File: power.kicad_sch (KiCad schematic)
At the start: 0 parts

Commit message: Connectors done, WIP on power
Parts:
- added C1: 100uF/16V, symbol Device:C_Polarized_Small
- added C10, C7: 0.1uF/50V, Capacitor_SMD:C_0603_1608Metric_Pad1.05x0.95mm_HandSolder, symbol Device:C
- added C11: 10pF/50V, Capacitor_SMD:C_0603_1608Metric_Pad1.05x0.95mm_HandSolder, symbol Device:C
- added C12, C13: 22uF/6.3V, Capacitor_Tantalum_SMD:CP_EIA-3216-10_Kemet-I_Pad1.58x1.35mm_HandSolder, symbol cellar-rescue:CP-Device
- added C2: 47nF/50V, symbol Device:C_Small
- added C3, C4: 1F / 8.1V, Capacitors:SCMR22J105SRBA0_vertical, symbol cellar-rescue:CP-Device
- added C5, C6: 10uF/25V, Capacitor_SMD:C_0805_2012Metric_Pad1.15x1.40mm_HandSolder, symbol Device:C
- added C8: 1uF/25V, Capacitor_SMD:C_0805_2012Metric_Pad1.15x1.40mm_HandSolder, symbol Device:C
- added C9: 8200pF/50V, Capacitor_SMD:C_0603_1608Metric_Pad1.05x0.95mm_HandSolder, symbol Device:C
- added D1: D, symbol Device:D
- added D2, D3, D4: SBR160S23-7, symbol Device:D
- added L1: 1.5uH, Inductors:L_7.1x6.5_H3, symbol cellar-rescue:INDUCTOR-pspice
- added Q1, Q2: Q_NPN_BEC, symbol Device:Q_NPN_BEC
- added R10: 22.1k, symbol Device:R
- added R11, R12: 30, symbol Device:R
- added R13, R3, R7, R9: 100k, symbol Device:R
- added R14: 124k 1%, symbol Device:R
- added R15: 22.1k 1%, symbol Device:R
- added R4, R8: 10k, symbol Device:R
- added R5: 37.4k, symbol Device:R
- added R6: 750k, symbol Device:R
- added U1: TLC555CDR, Package_SO:SOIC-8_3.9x4.9mm_P1.27mm, symbol Timer:TLC555xD
- added U2: L78L33ACUTR, Package_TO_SOT_SMD:SOT-89-3, symbol Regulator_Linear:L78L33_SOT89
- added U3: TPS54625, symbol power_custom:TPS54625
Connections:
- new net: C3.1, D4.2 (A), R11.1, R12.1
- new net: C3.2, C4.1
- new net: C11.2, R14.2, R15.1, U3.2 (VFB)
- new net: Q2.2 (E), R7.2, U1.4 (R)
- new net: Q2.3 (C), R8.1, U2.1 (OUT)
- new net: C10.1, U3.12 (VBST)
- new net: C10.2, L1.1, U3.10 (SW), U3.11 (SW)
- new net: C9.1, U3.4 (SS)
- new net: D2.1 (K), R11.2, R12.2
- new net: C2.1, U1.5 (CV)
- new net: D1.2 (A), R5.1, R6.2, U1.7 (DIS)
- new net: C8.1, R13.2, U3.3 (VREG5)
- new net: R13.1, U3.6 (PG)
- new net: R4.1, U1.3 (Q)
- new net: Q1.1 (B), R4.2
- new net +12V: D2.2 (A), D3.2 (A), R9.1, U2.3 (IN)
- new net +5V: C11.1, C12.1, C13.1, L1.2, R14.1, U3.1 (VO)
- new net ENABLE: Q1.3 (C), R3.2, U3.7 (EN)
- new net GND: C1.2, C12.2, C13.2, C2.2, C4.2, C5.2, C6.2, C7.2, C8.2, C9.2, Q1.2 (E), R10.2, R15.2, R7.1, U1.1 (GND), U2.2 (GND), U3.15 (GND), U3.5 (GND), U3.8 (GND), U3.9 (GND)
- new net POWER_STATE: R10.1, R9.2
- new net THR: C1.1, D1.1 (K), R6.1, U1.2 (TR), U1.6 (THR)
- new net VCOND: C5.1, C6.1, C7.1, D3.1 (K), D4.1 (K), R3.1, R5.2, U1.8 (VCC), U3.13 (VIN), U3.14 (VIN)
- new net WATCHDOG: Q2.1 (B), R8.2
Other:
- note added: "555"

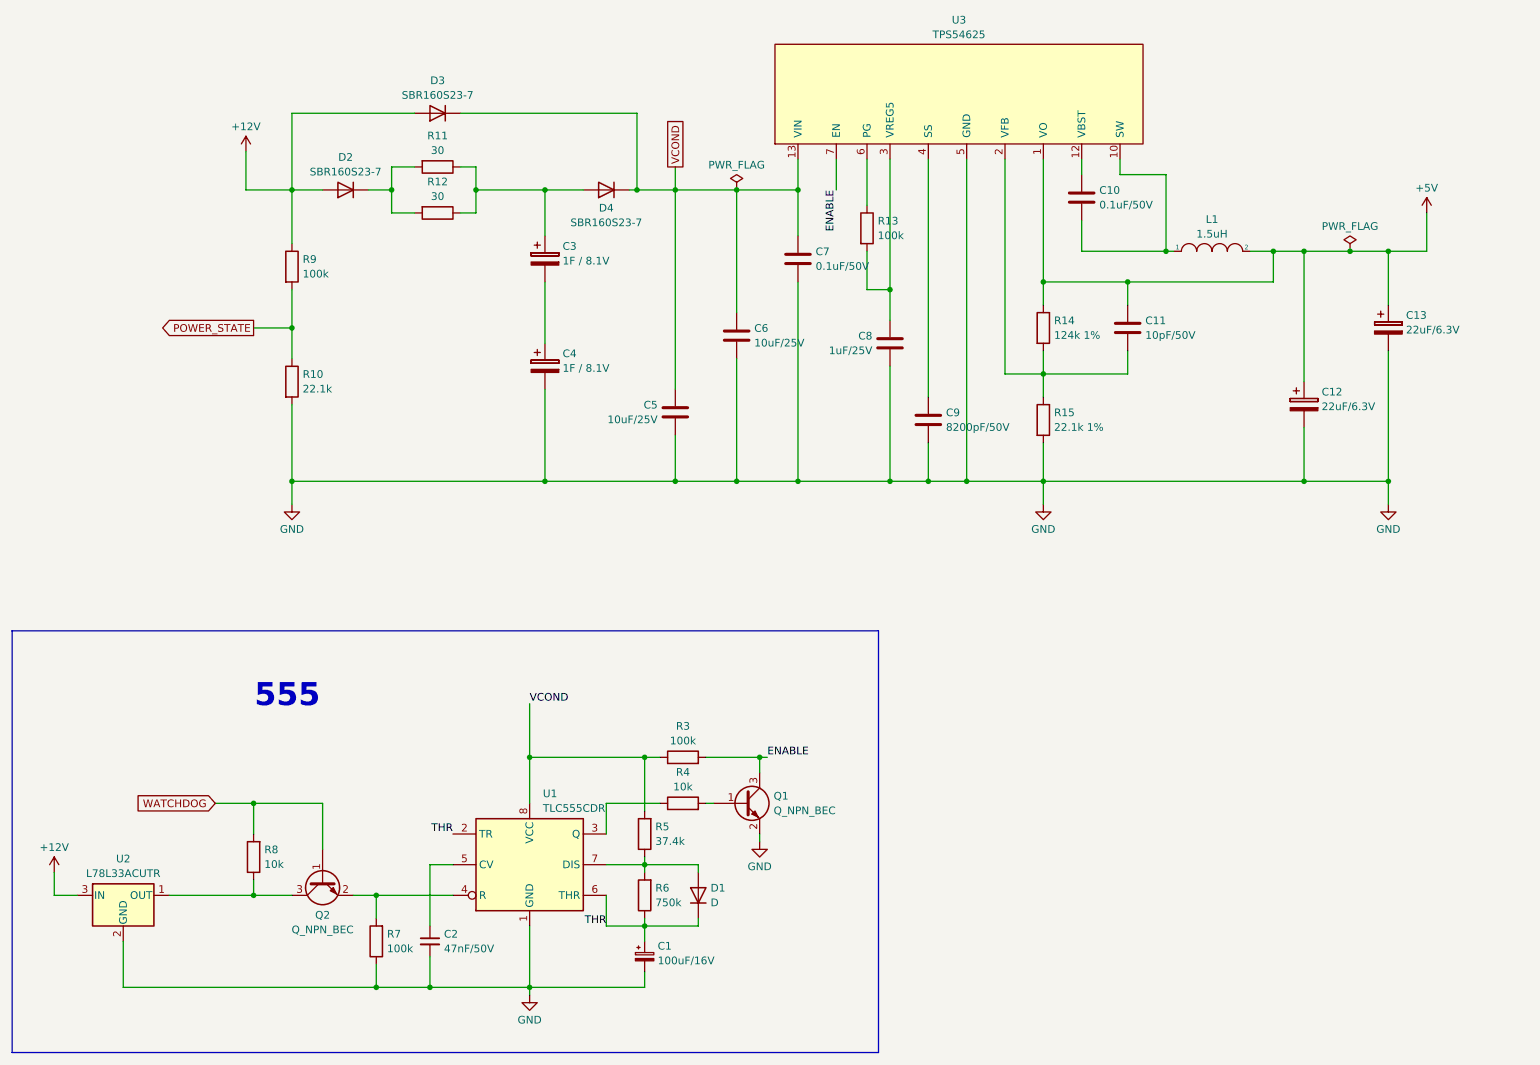
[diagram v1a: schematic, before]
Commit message: Schematic done (for now), WIP on layout
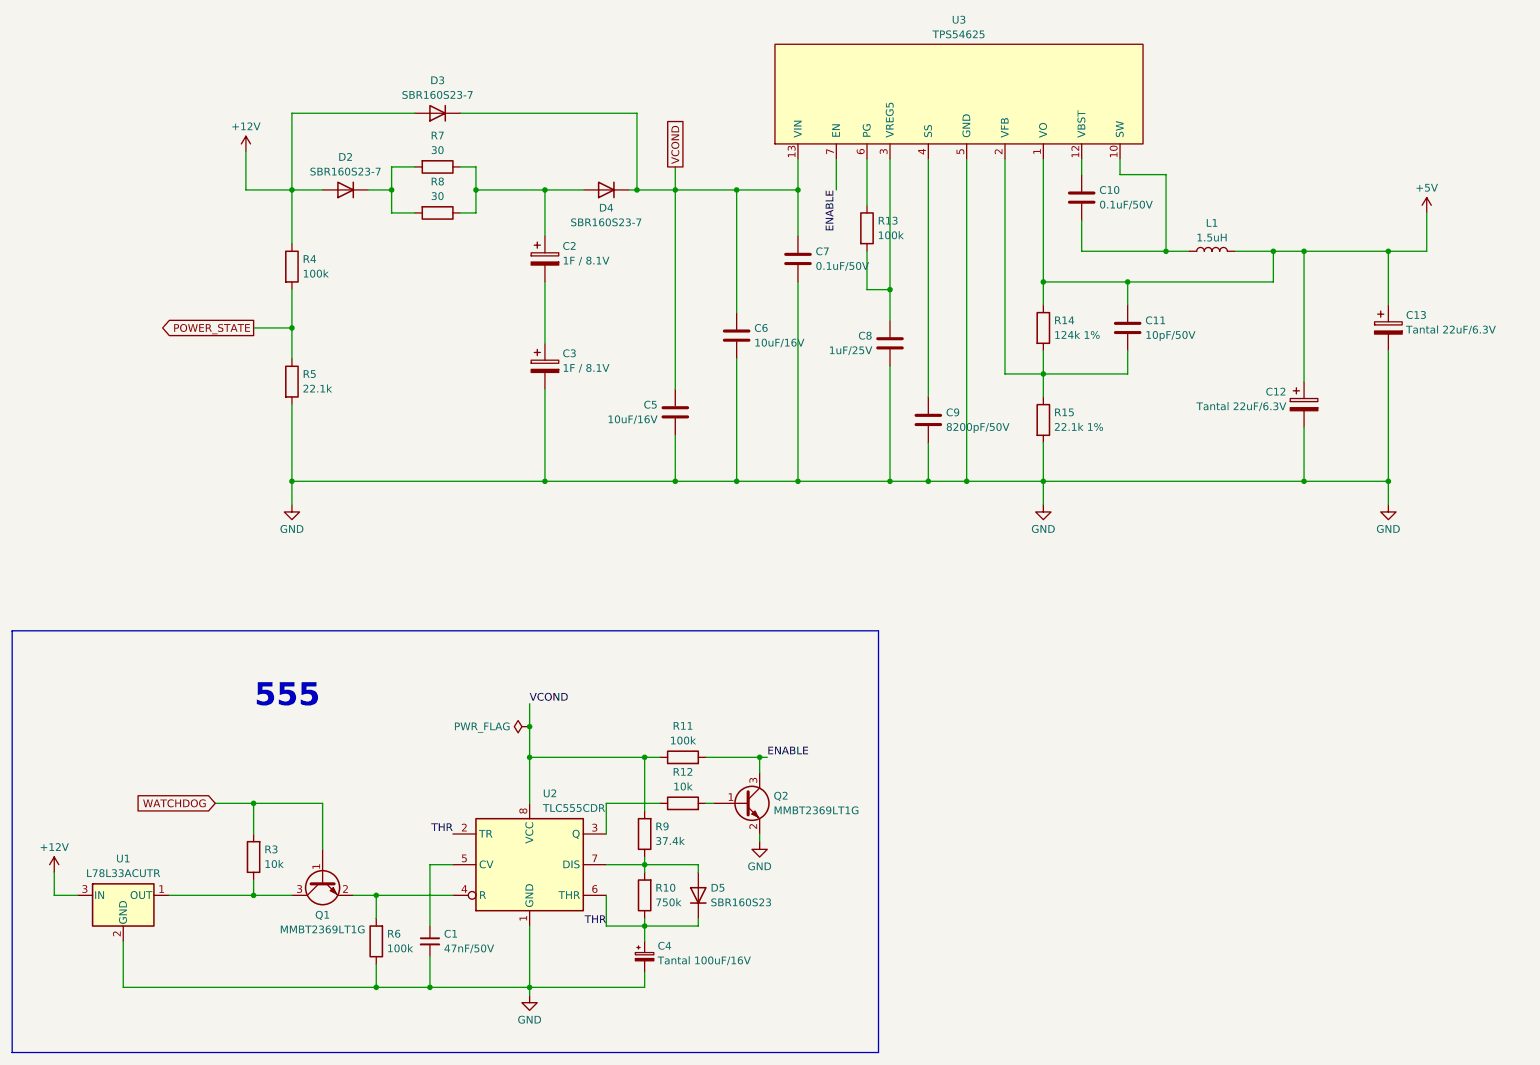
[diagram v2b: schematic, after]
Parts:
- removed Q2: Q_NPN_BEC, symbol Device:Q_NPN_BEC
- added Q1: MMBT2369LT1G, Package_TO_SOT_SMD:SOT-23_Handsoldering, symbol Device:Q_NPN_BEC
- C1: renamed from C2; footprint (none) -> Capacitor_SMD:C_0603_1608Metric_Pad1.08x0.95mm_HandSolder
- C10, C11, C7, C9: footprint Capacitor_SMD:C_0603_1608Metric_Pad1.05x0.95mm_HandSolder -> Capacitor_SMD:C_0603_1608Metric_Pad1.08x0.95mm_HandSolder
- C12, C13: value 22uF/6.3V -> Tantal 22uF/6.3V; symbol cellar-rescue:CP-Device -> Device:C_Polarized
- C2: renamed from C3; symbol cellar-rescue:CP-Device -> Device:C_Polarized; Ref SCMR22J105SRBA0 -> SCMR22G105SRBA0
- C3: renamed from C4; symbol cellar-rescue:CP-Device -> Device:C_Polarized; Ref SCMR22J105SRBA0 -> SCMR22G105SRBA0
- C4: renamed from C1; value 100uF/16V -> Tantal 100uF/16V; footprint (none) -> Capacitor_Tantalum_SMD:CP_EIA-7343-30_AVX-N_Pad2.25x2.55mm_HandSolder
- C5, C6: value 10uF/25V -> 10uF/16V; footprint Capacitor_SMD:C_0805_2012Metric_Pad1.15x1.40mm_HandSolder -> Capacitor_SMD:C_0805_2012Metric_Pad1.18x1.45mm_HandSolder
- C8: footprint Capacitor_SMD:C_0805_2012Metric_Pad1.15x1.40mm_HandSolder -> Capacitor_SMD:C_0603_1608Metric_Pad1.08x0.95mm_HandSolder
- D2, D3, D4: footprint (none) -> Diodes_custom:SBR160S23
- D5: renamed from D1; value D -> SBR160S23; footprint (none) -> Diodes_custom:SBR160S23
- L1: symbol cellar-rescue:INDUCTOR-pspice -> Device:L
- Q2: renamed from Q1; value Q_NPN_BEC -> MMBT2369LT1G; footprint (none) -> Package_TO_SOT_SMD:SOT-23_Handsoldering
- R10: renamed from R6; footprint (none) -> Resistor_SMD:R_0603_1608Metric_Pad0.98x0.95mm_HandSolder
- R11: renamed from R3; footprint (none) -> Resistor_SMD:R_0603_1608Metric_Pad0.98x0.95mm_HandSolder
- R12: renamed from R4; footprint (none) -> Resistor_SMD:R_0603_1608Metric_Pad0.98x0.95mm_HandSolder
- R13, R14, R15: footprint (none) -> Resistor_SMD:R_0603_1608Metric_Pad0.98x0.95mm_HandSolder
- R3: renamed from R8; footprint (none) -> Resistor_SMD:R_0603_1608Metric_Pad0.98x0.95mm_HandSolder
- R4: renamed from R9; footprint (none) -> Resistor_SMD:R_0603_1608Metric_Pad0.98x0.95mm_HandSolder
- R5: renamed from R10; footprint (none) -> Resistor_SMD:R_0603_1608Metric_Pad0.98x0.95mm_HandSolder
- R6: renamed from R7; footprint (none) -> Resistor_SMD:R_0603_1608Metric_Pad0.98x0.95mm_HandSolder
- R7: renamed from R11; footprint (none) -> Resistors_custom:TE_SM5
- R8: renamed from R12; footprint (none) -> Resistors_custom:TE_SM5
- R9: renamed from R5; footprint (none) -> Resistor_SMD:R_0603_1608Metric_Pad0.98x0.95mm_HandSolder
- U1: renamed from U2; footprint Package_TO_SOT_SMD:SOT-89-3 -> Package_TO_SOT_SMD:SOT-89-3_Handsoldering
- U3: footprint (none) -> TexasInstruments:HTSSOP-14-PWP_Handsolder
- renumbered U1 to U2
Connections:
- net WATCHDOG: now also Q1.1 (B)
- net at R6.2, U2.4 (R): now also Q1.2 (E)
- net at R3.1, U1.1 (OUT): now also Q1.3 (C)

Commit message: All done, pending review
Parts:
- C2, C3: footprint Capacitors:SCMR22J105SRBA0_vertical -> Capacitors:SCMR22G105SRBA0_vertical
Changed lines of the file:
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@@
 			)
 		)
-		(property "Footprint" "Capacitors:SCMR22J105SRBA0_vertical"
+		(property "Footprint" "Capacitors:SCMR22G105SRBA0_vertical"
 			(at 113.9952 62.23 0)
 			(effects
@@
 			)
 		)
-		(property "Footprint" "Capacitors:SCMR22J105SRBA0_vertical"
+		(property "Footprint" "Capacitors:SCMR22G105SRBA0_vertical"
 			(at 113.9952 80.01 0)
 			(effects
